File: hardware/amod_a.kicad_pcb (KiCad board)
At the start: 4 copper layers, 100 x 100 mm, 50 parts, among them J101 USB-C, J102 rails, J201 SMA, J202 SMA, J301 SMA, J302 SMA, Q201 AO3401A, Q301 AO3401A, SW201 ON, SW301 ON, U101 LM2664, U102 3.3V, U201 OPA810, U301 OPA810

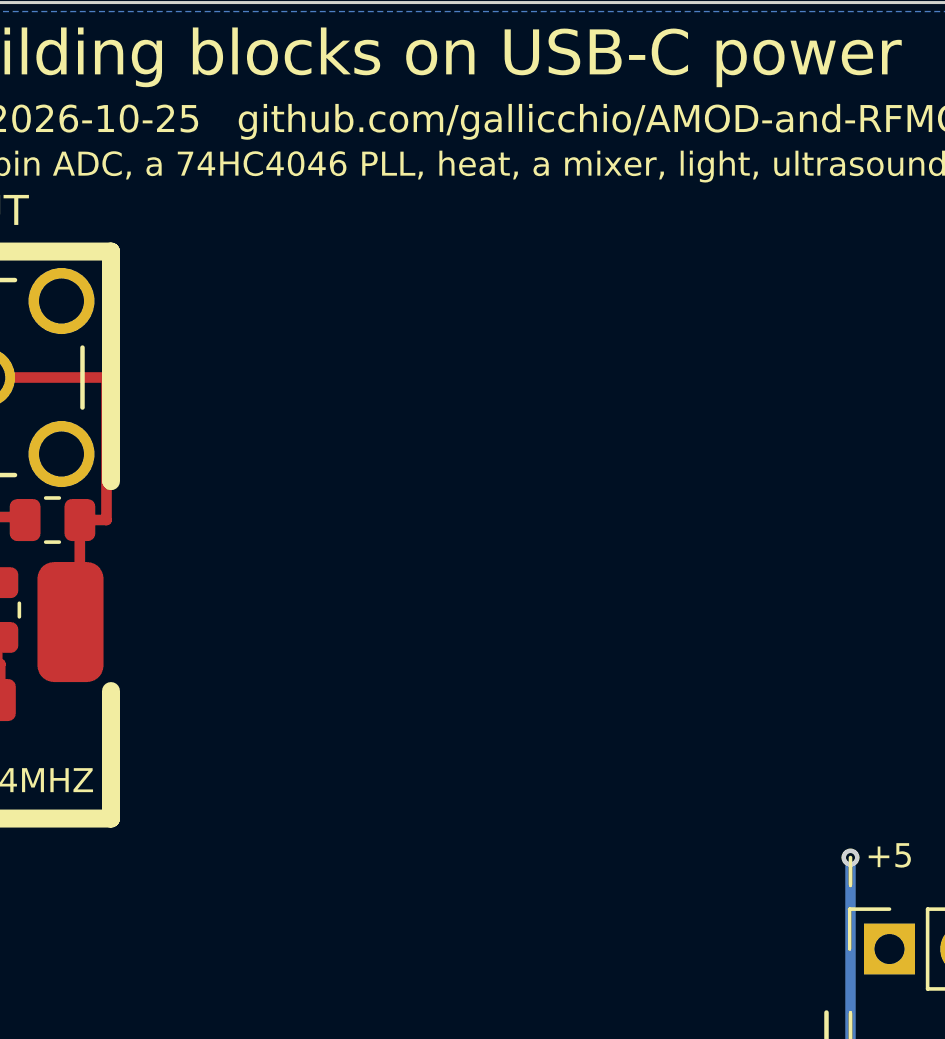
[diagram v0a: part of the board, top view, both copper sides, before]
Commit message: AMOD-A A4: the OPA847 LNA at DRC 0 (feedback through the NC pin, VS on the back, own SOIC-8 symbol)
Co-Authored-By: Claude Fable 5.1 <noreply@anthropic.com>
Claude-Session: https://claude.ai/code/session_01RKeoKvFFzjk3cEBLCXXHnB
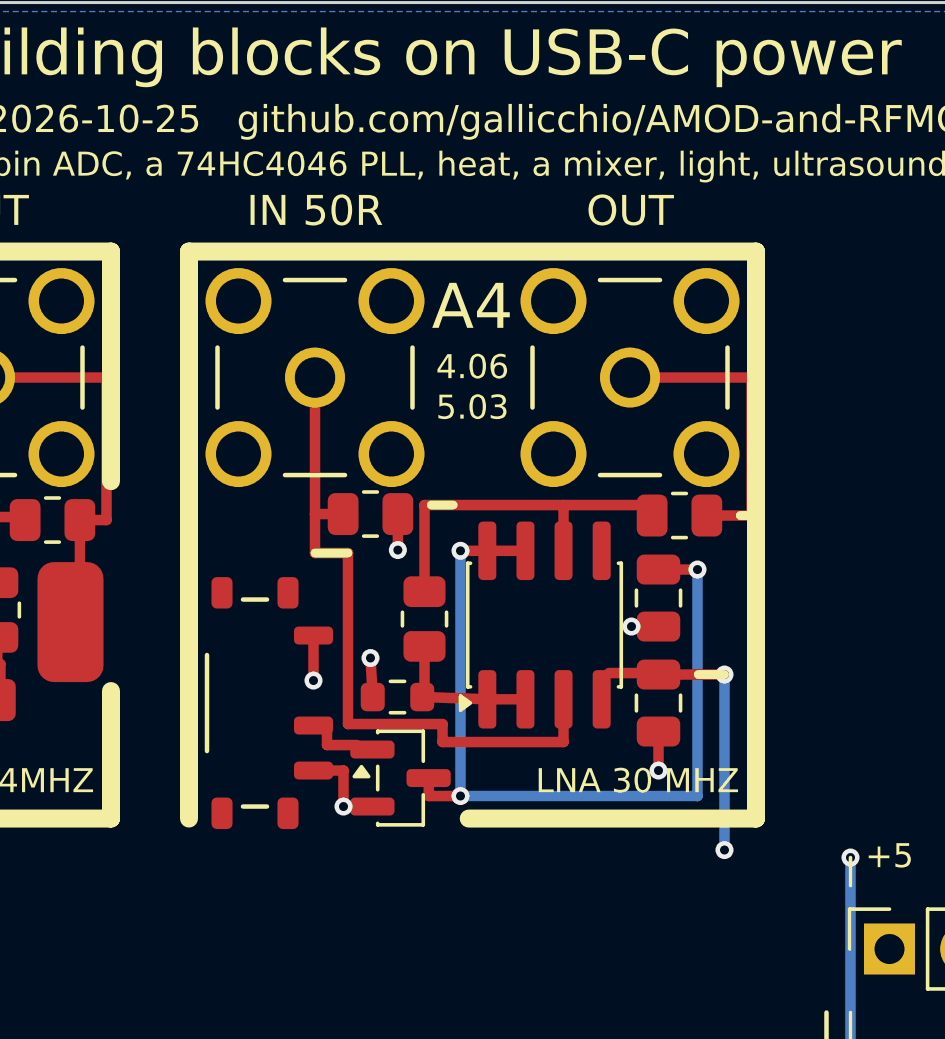
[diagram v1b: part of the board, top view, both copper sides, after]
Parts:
- added C401: 100n, Capacitor_SMD:C_0805_2012Metric, F.Cu at (67.0, 19.9)
- added C402: 100n, Capacitor_SMD:C_0805_2012Metric, F.Cu at (67.0, 23.4)
- added J401: SMA, amod:SMA_BWSMA-KE-Z001_Vertical, F.Cu at (55.5, 12.5)
- added J402: SMA, amod:SMA_BWSMA-KE-Z001_Vertical, F.Cu at (66.0, 12.5)
- added Q401: AO3401A, Package_TO_SOT_SMD:SOT-23, F.Cu at (58.4, 25.9)
- added R401: 49.9, Resistor_SMD:R_0805_2012Metric, F.Cu at (57.4, 17.1)
- added R402: 1k, Resistor_SMD:R_0805_2012Metric, F.Cu at (59.1, 20.6)
- added R403: 10R, Resistor_SMD:R_0603_1608Metric, F.Cu at (58.2, 23.1)
- added R404: 49.9, Resistor_SMD:R_0805_2012Metric, F.Cu at (67.7, 17.1)
- added SW401: ON, amod:SW_SPDT_Shouhan_MSK12C02, F.Cu at (53.5, 23.4)
- added U401: OPA847, Package_SO:SOIC-8_3.9x4.9mm_P1.27mm, F.Cu at (63.1, 20.8)
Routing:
- net /A4_VS: track 0.00 -> 28.7 mm, vias 0 -> 3
- net /A4_IN: track 0.00 -> 22.8 mm
- net /A4_OUT_A: track 0.00 -> 12.4 mm
- net /A4_OUT: track 0.00 -> 10.1 mm
- net -5V: track 43.8 -> 52.9 mm, vias 8 -> 10
- net GND: track 37.3 -> 43.5 mm, vias 26 -> 31
- net /A4_FB: track 0.00 -> 5.13 mm
- net +5V: track 31.0 -> 34.2 mm, vias 5 -> 6
- net /A4_G: track 0.00 -> 1.40 mm
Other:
- board text added: "5.03"
- board text added: "A4"
- board text added: "LNA 30 MHZ"

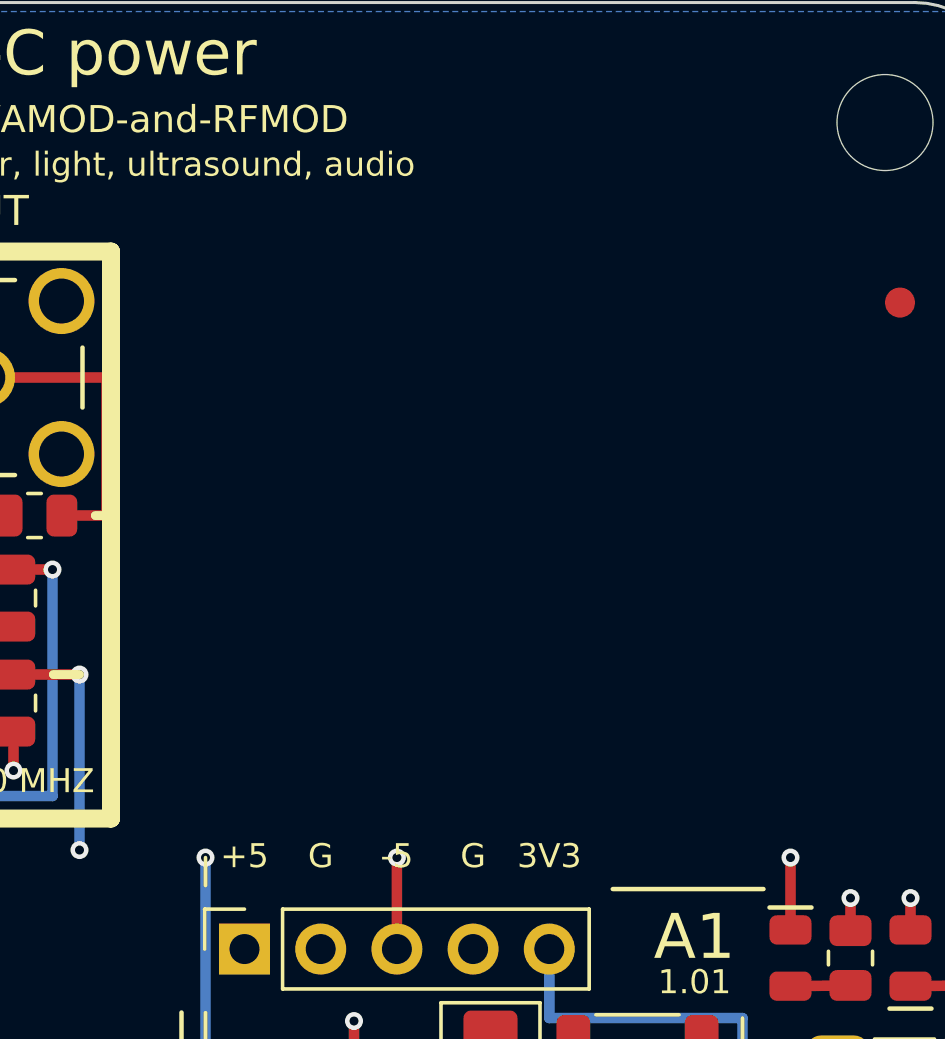
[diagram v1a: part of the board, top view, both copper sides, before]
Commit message: AMOD-A A5: Johnson noise on an LT6230 (1.1 nV) in the A2 geometry, 10k / 1k by DIP or a socketed resistor, DRC 0
Co-Authored-By: Claude Fable 5.1 <noreply@anthropic.com>
Claude-Session: https://claude.ai/code/session_01RKeoKvFFzjk3cEBLCXXHnB
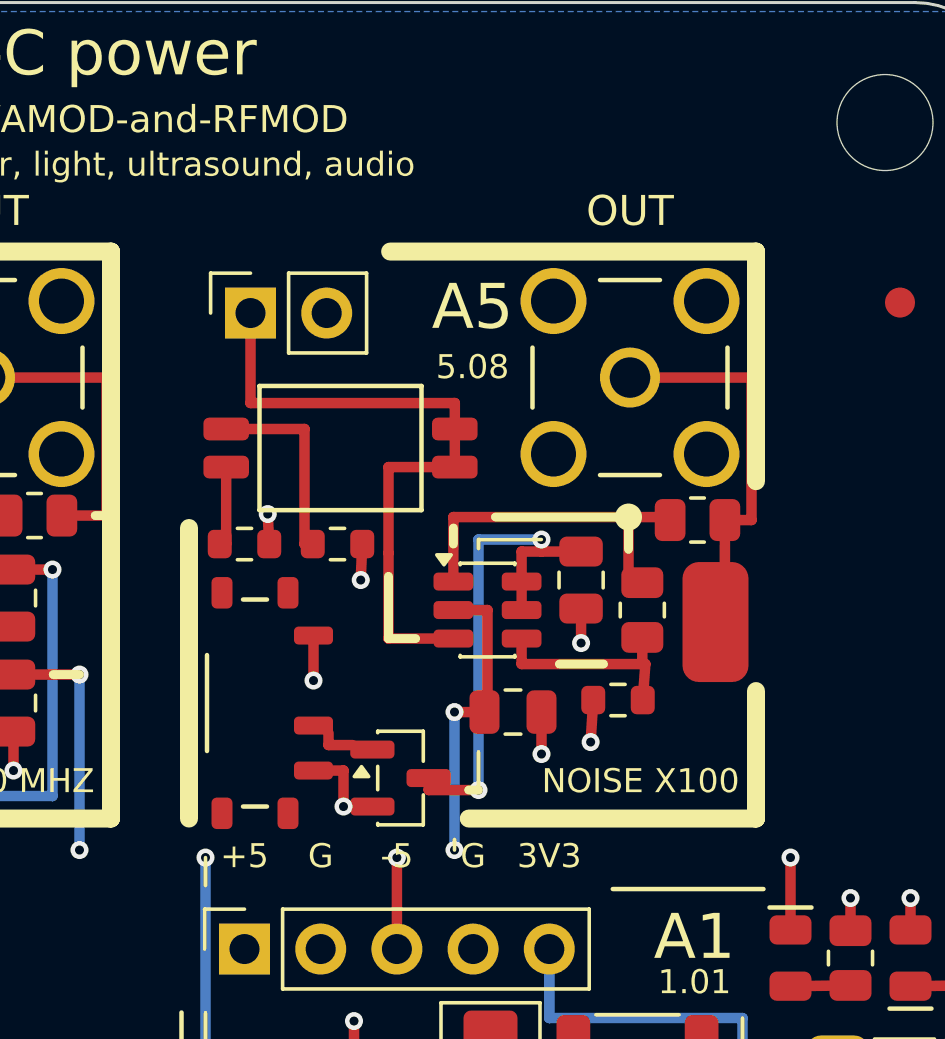
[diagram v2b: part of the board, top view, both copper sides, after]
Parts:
- added C501: 100n, Capacitor_SMD:C_0805_2012Metric, F.Cu at (85.9, 19.2)
- added C502: 100n, Capacitor_SMD:C_0805_2012Metric, F.Cu at (83.6, 23.6)
- added J501: SMA, amod:SMA_BWSMA-KE-Z001_Vertical, F.Cu at (87.5, 12.5)
- added J502: R, Connector_PinSocket_2.54mm:PinSocket_1x02_P2.54mm_Vertical, F.Cu at (74.8, 10.3)
- added Q501: AO3401A, Package_TO_SOT_SMD:SOT-23, F.Cu at (79.8, 25.9)
- added R501: 10k, Resistor_SMD:R_0603_1608Metric, F.Cu at (74.7, 18.1)
- added R502: 1k, Resistor_SMD:R_0603_1608Metric, F.Cu at (77.8, 18.1)
- added R503: 1k, Resistor_SMD:R_0805_2012Metric, F.Cu at (87.9, 20.2)
- added R504: 10R, Resistor_SMD:R_0603_1608Metric, F.Cu at (87.1, 23.2)
- added R505: 49.9, Resistor_SMD:R_0805_2012Metric, F.Cu at (89.8, 17.2)
- added SW501: ON, amod:SW_SPDT_Shouhan_MSK12C02, F.Cu at (75.0, 23.4)
- added SW502: DIP2, amod:SW_DIP_SPSTx02_Slide_1.27mm_DSHP02, F.Cu at (77.8, 14.8)
- added TP501: OUT, amod:TestPoint_Loop_RH-5019, F.Cu at (90.3, 20.6)
- added U501: LT6230, Package_TO_SOT_SMD:SOT-23-6, F.Cu at (82.8, 20.2)
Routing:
- net /A5_IN: track 0.00 -> 22.0 mm
- net /A5_VS: track 0.00 -> 16.8 mm, vias 0 -> 2
- net /A5_OUT: track 0.00 -> 13.4 mm
- net /A5_OUT_A: track 0.00 -> 12.1 mm
- net -5V: track 52.9 -> 63.1 mm, vias 10 -> 12
- net GND: track 43.5 -> 51.1 mm, vias 31 -> 37
- net /A5_FB: track 0.00 -> 7.07 mm
- net /A5_R1K: track 0.00 -> 6.72 mm
- net +5V: track 34.2 -> 37.3 mm, vias 6 -> 7
- net /A5_R10K: track 0.00 -> 2.78 mm
- net /A5_G: track 0.00 -> 1.20 mm
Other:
- board text added: "5.08"
- board text added: "A5"
- board text added: "NOISE X100"

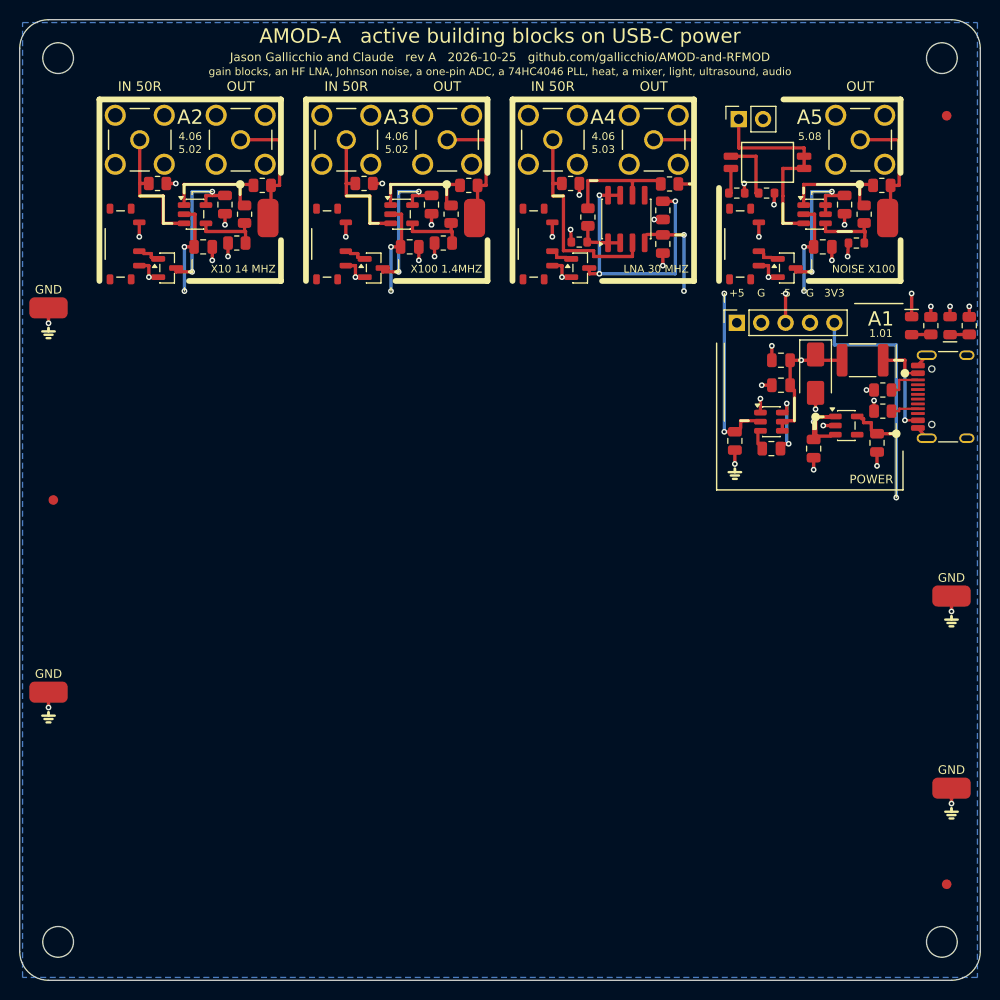
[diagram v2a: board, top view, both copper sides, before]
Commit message: AMOD-A A6 (delta-sigma), A8 (heater), A11 (ultrasound + the Pmod plug and lines) at DRC 0; the op-amp geometry takes an offset
- +3.3 V tiles' header via in the gutter below; board-level back wires; the QR and back text per board
- the schematic joins adjacent same-net pins with one label

Co-Authored-By: Claude Fable 5.1 <noreply@anthropic.com>
Claude-Session: https://claude.ai/code/session_01RKeoKvFFzjk3cEBLCXXHnB
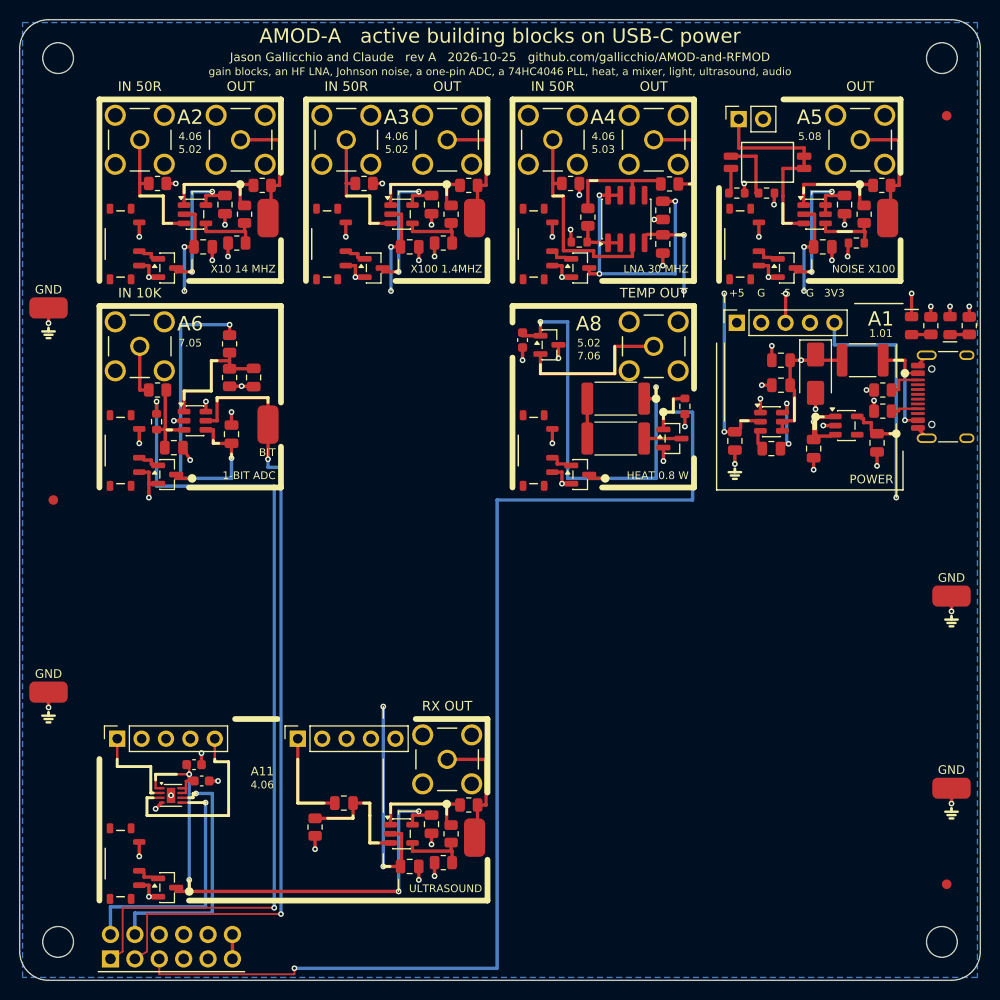
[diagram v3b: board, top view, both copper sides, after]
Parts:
- added C1101: 100n, Capacitor_SMD:C_0603_1608Metric, F.Cu at (18.9, 79.2)
- added C1102: 100n, Capacitor_SMD:C_0603_1608Metric, F.Cu at (18.1, 77.5)
- added C1103: 10n, Capacitor_SMD:C_0805_2012Metric, F.Cu at (33.8, 81.5)
- added C1104: 100n, Capacitor_SMD:C_0805_2012Metric, F.Cu at (42.9, 83.8)
- added C1105: 100n, Capacitor_SMD:C_0805_2012Metric, F.Cu at (40.6, 88.2)
- added C601: 10n, Capacitor_SMD:C_0805_2012Metric, F.Cu at (16.1, 44.5)
- added C602: 100n, Capacitor_SMD:C_0805_2012Metric, F.Cu at (22.1, 43.1)
- added C603: 100n, Capacitor_SMD:C_0805_2012Metric, F.Cu at (24.4, 37.2)
- added C801: 100n, Capacitor_SMD:C_0603_1608Metric, F.Cu at (52.4, 33.4)
- added J1101: SMA, amod:SMA_BWSMA-KE-Z001_Vertical, F.Cu at (44.5, 77.0)
- added J1102: TX, Connector_PinSocket_2.54mm:PinSocket_1x05_P2.54mm_Vertical, F.Cu at (10.2, 74.8)
- added J1103: RX, Connector_PinSocket_2.54mm:PinSocket_1x05_P2.54mm_Vertical, F.Cu at (28.9, 74.8)
- added J1104: Pmod, amod:PinHeader_2x06_P2.54mm_Horizontal_PZ254R-12-12P, F.Cu at (15.8, 96.5)
- added J601: SMA, amod:SMA_BWSMA-KE-Z001_Vertical, F.Cu at (12.5, 34.0)
- added J801: SMA, amod:SMA_BWSMA-KE-Z001_Vertical, F.Cu at (66.0, 34.0)
- added Q1101: AO3401A, Package_TO_SOT_SMD:SOT-23, F.Cu at (15.3, 90.3)
- added Q601: AO3401A, Package_TO_SOT_SMD:SOT-23, F.Cu at (15.3, 47.4)
- added Q801: AO3401A, Package_TO_SOT_SMD:SOT-23, F.Cu at (58.4, 47.4)
- added Q802: AO3400A, Package_TO_SOT_SMD:SOT-23, F.Cu at (68.0, 43.6)
- added R1101: 3.9k, Resistor_SMD:R_0805_2012Metric, F.Cu at (30.8, 84.0)
- added R1102: 10k, Resistor_SMD:R_0805_2012Metric, F.Cu at (44.9, 84.8)
- added R1103: 100R, Resistor_SMD:R_0805_2012Metric, F.Cu at (44.1, 87.8)
- added R1104: 49.9, Resistor_SMD:R_0805_2012Metric, F.Cu at (46.8, 81.8)
- added R601: 10k, Resistor_SMD:R_0805_2012Metric, F.Cu at (14.3, 38.5)
- added R602: 10k, Resistor_SMD:R_0603_1608Metric, F.Cu at (14.2, 41.9)
- added R603: 10k, Resistor_SMD:R_0805_2012Metric, F.Cu at (21.9, 33.8)
- added R604: 10k, Resistor_SMD:R_0805_2012Metric, F.Cu at (21.9, 37.2)
- added R801: 15R, Resistor_SMD:R_2512_6332Metric, F.Cu at (62.0, 39.5)
- added R802: 15R, Resistor_SMD:R_2512_6332Metric, F.Cu at (62.0, 43.6)
- added R803: 10k, Resistor_SMD:R_0603_1608Metric, F.Cu at (69.2, 40.2)
- added SW1101: ON, amod:SW_SPDT_Shouhan_MSK12C02, F.Cu at (10.5, 87.8)
- added SW601: ON, amod:SW_SPDT_Shouhan_MSK12C02, F.Cu at (10.5, 44.9)
- added SW801: ON, amod:SW_SPDT_Shouhan_MSK12C02, F.Cu at (53.5, 44.9)
- added TP1101: OUT, amod:TestPoint_Loop_RH-5019, F.Cu at (47.4, 85.2)
- added TP601: BIT, amod:TestPoint_Loop_RH-5019, F.Cu at (25.9, 42.1)
- added U1101: DRV8837, Package_SON:Texas_DSG0008A_WSON-8-1EP_2x2mm_P0.5mm_EP0.9x1.6mm, F.Cu at (15.8, 80.8)
- added U1102: OPA810, Package_TO_SOT_SMD:SOT-23-5, F.Cu at (39.8, 84.8)
- added U601: TLV3501, Package_TO_SOT_SMD:SOT-23-6, F.Cu at (18.2, 41.8)
- added U801: TMP235, Package_TO_SOT_SMD:SOT-23, F.Cu at (55.1, 33.9)
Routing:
- net /PMOD3: track 0.00 -> 124.1 mm, vias 0 -> 2
- net /PMOD1: track 0.00 -> 88.0 mm, vias 0 -> 2
- net /PMOD2: track 0.00 -> 83.3 mm, vias 0 -> 2
- net /A11_VS: track 0.00 -> 60.8 mm, vias 0 -> 4
- net /A8_VS: track 0.00 -> 46.0 mm, vias 0 -> 3
- net /A6_VS: track 0.00 -> 37.3 mm, vias 0 -> 3
- net /PMOD6: track 0.00 -> 26.5 mm, vias 0 -> 1
- net /PMOD5: track 0.00 -> 26.3 mm, vias 0 -> 1
- net GND: track 51.1 -> 76.9 mm, vias 37 -> 57
- net -5V: track 63.1 -> 86.2 mm, vias 12 -> 14
- net /A11_OUT2: track 0.00 -> 21.3 mm
- net /A8_OUT: track 0.00 -> 16.7 mm
- net /A6_VREF: track 0.00 -> 14.3 mm
- net /A11_IN: track 0.00 -> 13.6 mm
- net /A11_OUT: track 0.00 -> 13.4 mm
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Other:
- board text added: "1-BIT ADC"
- board text added: "7.05"
- board text added: "7.06"
- board text added: "A11"
- board text added: "A6"
- board text added: "A8"
- board text added: "AMOD-A: active blocks on USB-C power. Each tile"
- board text added: "BIT"
- board text added: "DAC OUT to IN, OUT to ADC IN. The Pmod plug (left)"
- board text added: "HEAT 0.8 W"
- board text added: "IN 10K"
- board text added: "RX OUT"
- board text added: "TEMP OUT"
- board text added: "ULTRASOUND"
- board text added: "has a slide switch (up: on) and SMA jacks: cable"
- board text added: "takes the FPGA's lines; the handbook has the rest."
- board text removed: "AMOD-A: active building blocks on USB-C power. Each tile has its own slide switch (slider up: on) and SMA jacks;"
- board text removed: "cable DAC OUT to a tile's IN and its OUT to ADC IN. The inputs take what the tile's silk says. The power tile's socket (top edge)"
- board text removed: "carries +5, ground, -5, ground, +3.3 V. The handbook has each tile's expected response and its Pmod pins."
